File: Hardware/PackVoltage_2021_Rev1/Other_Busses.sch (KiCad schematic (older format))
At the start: 50 parts, among them Q10 Q_NMOS_DGS, Q6 Q_NMOS_DGS, Q7 Q_NMOS_DGS, Q8 Q_NMOS_DGS, Q9 Q_NMOS_DGS, U14 LT1910, U15 LT1910, U16 LT1910, U17 INA281, U18 INA281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

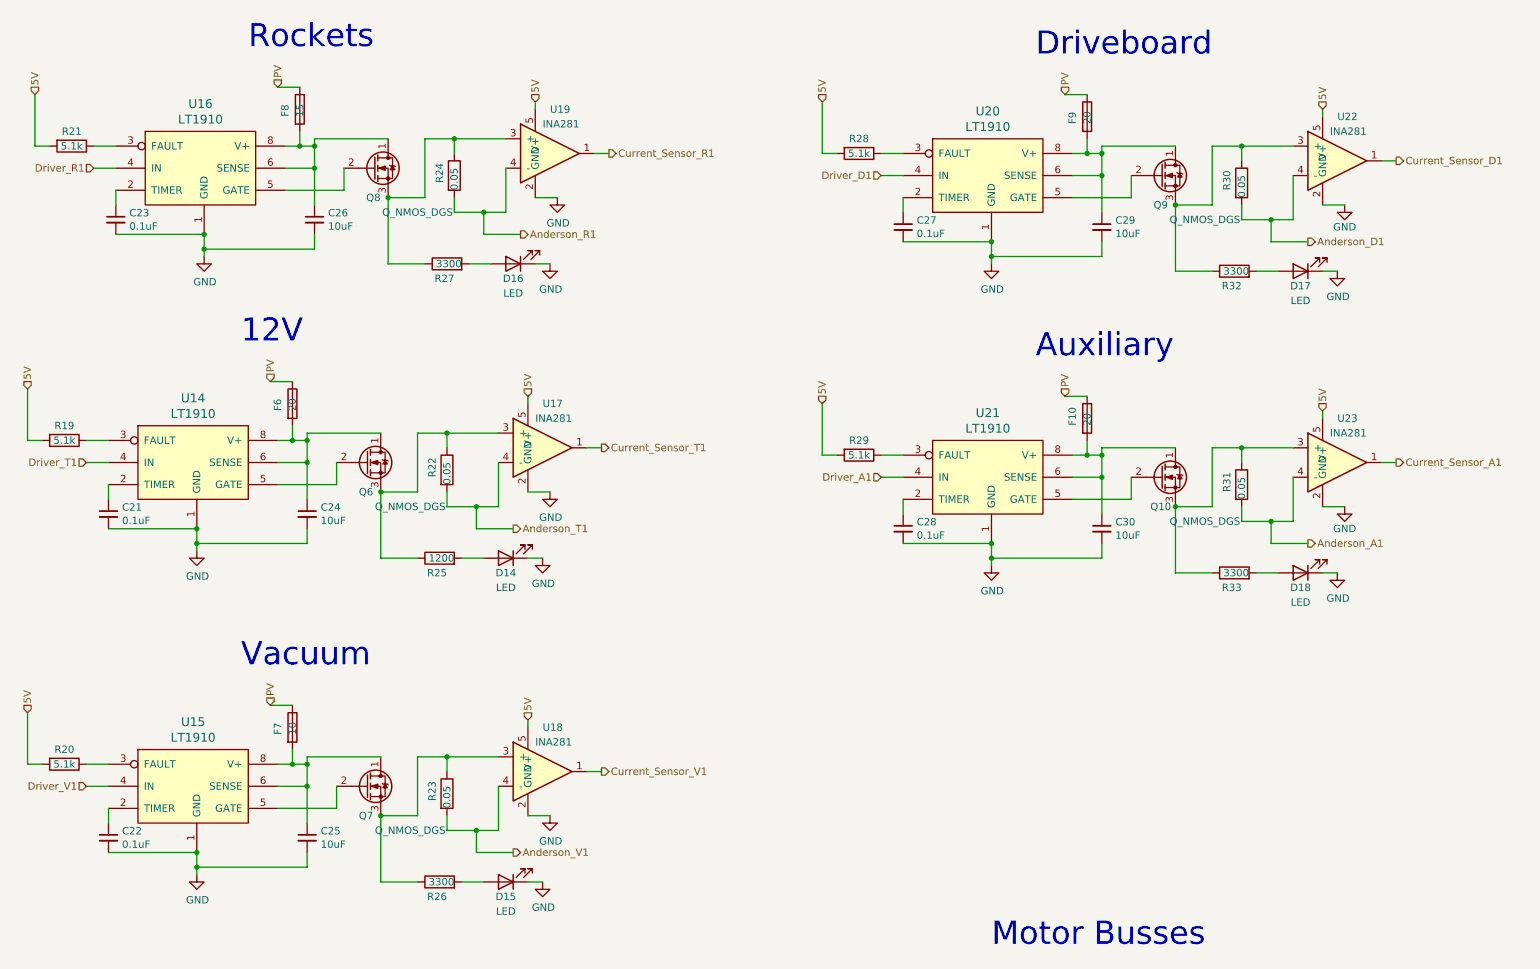
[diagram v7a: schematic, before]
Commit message: Updated 12 Molex, Changed Shunt Resistors
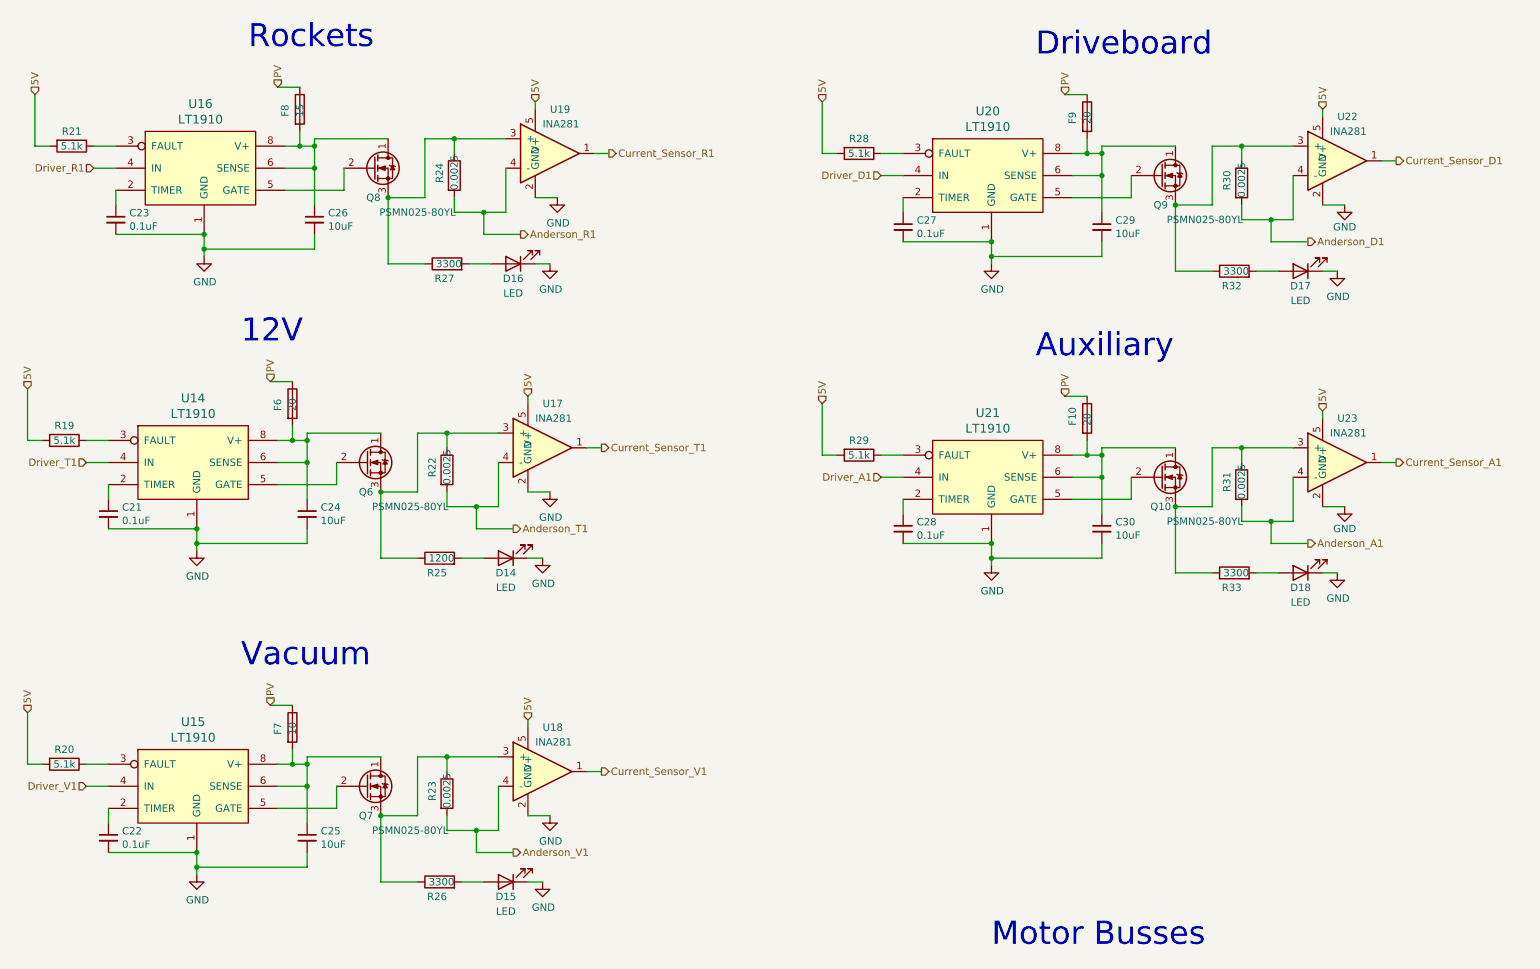
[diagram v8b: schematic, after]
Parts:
- Q10, Q6, Q7, Q8, Q9: value Q_NMOS_DGS -> PSMN025-80YL
- R22, R23, R24, R30, R31: value 0.05 -> 0.0025; footprint Resistor_SMD:R_2512_6332Metric_Pad1.40x3.35mm_HandSolder -> Resistor_SMD:R_2512_6332Metric_Pad1.52x3.35mm_HandSolder
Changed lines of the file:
@@
 AR Path="/5F8EFCC9/5F768EE8" Ref="Q8"  Part="1"
 F 0 "Q8" H 3000 1450 50  0000 C CNN
-F 1 "Q_NMOS_DGS" H 3300 1350 50  0000 C CNN
+F 1 "PSMN025-80YL" H 3300 1350 50  0000 C CNN
 F 2 "Custom:LFPAK56_MOSFET" H 3200 1750 50  0001 C CNN
 F 3 "~" H 3000 1650 50  0001 C CNN
@@
 AR Path="/5F8EFCC9/5F9AF790" Ref="R24"  Part="1"
 F 0 "R24" V 3450 1650 50  0000 L CNN
-F 1 "0.05" V 3550 1600 50  0000 L CNN
-F 2 "Resistor_SMD:R_2512_6332Metric_Pad1.40x3.35mm_HandSolder" V 3480 1700 50  0001 C CNN
+F 1 "0.0025" V 3550 1600 50  0000 L CNN
+F 2 "Resistor_SMD:R_2512_6332Metric_Pad1.52x3.35mm_HandSolder" V 3480 1700 50  0001 C CNN
 F 3 "https://riedon.com/media/pdf/PFS35.pdf" H 3550 1700 50  0001 C CNN
 	1    3550 1700
@@
 AR Path="/5F8EFCC9/5F9AF794" Ref="Q6"  Part="1"
 F 0 "Q6" H 2950 3450 50  0000 C CNN
-F 1 "Q_NMOS_DGS" H 3250 3350 50  0000 C CNN
+F 1 "PSMN025-80YL" H 3250 3350 50  0000 C CNN
 F 2 "Custom:LFPAK56_MOSFET" H 3150 3750 50  0001 C CNN
 F 3 "~" H 2950 3650 50  0001 C CNN
@@
 AR Path="/5F8EFCC9/5F9AF79A" Ref="R22"  Part="1"
 F 0 "R22" V 3400 3650 50  0000 L CNN
-F 1 "0.05" V 3500 3600 50  0000 L CNN
-F 2 "Resistor_SMD:R_2512_6332Metric_Pad1.40x3.35mm_HandSolder" V 3430 3700 50  0001 C CNN
+F 1 "0.0025" V 3500 3600 50  0000 L CNN
+F 2 "Resistor_SMD:R_2512_6332Metric_Pad1.52x3.35mm_HandSolder" V 3430 3700 50  0001 C CNN
 F 3 "https://riedon.com/media/pdf/PFS35.pdf" H 3500 3700 50  0001 C CNN
 	1    3500 3700
@@
 AR Path="/5F8EFCC9/5F9AF7A1" Ref="Q7"  Part="1"
 F 0 "Q7" H 2950 5650 50  0000 C CNN
-F 1 "Q_NMOS_DGS" H 3250 5550 50  0000 C CNN
+F 1 "PSMN025-80YL" H 3250 5550 50  0000 C CNN
 F 2 "Custom:LFPAK56_MOSFET" H 3150 5950 50  0001 C CNN
 F 3 "~" H 2950 5850 50  0001 C CNN
@@
 AR Path="/5F8EFCC9/5F8A5A13" Ref="R23"  Part="1"
 F 0 "R23" V 3400 5850 50  0000 L CNN
-F 1 "0.05" V 3500 5800 50  0000 L CNN
-F 2 "Resistor_SMD:R_2512_6332Metric_Pad1.40x3.35mm_HandSolder" V 3430 5900 50  0001 C CNN
+F 1 "0.0025" V 3500 5800 50  0000 L CNN
+F 2 "Resistor_SMD:R_2512_6332Metric_Pad1.52x3.35mm_HandSolder" V 3430 5900 50  0001 C CNN
 F 3 "https://riedon.com/media/pdf/PFS35.pdf" H 3500 5900 50  0001 C CNN
 	1    3500 5900
@@
 AR Path="/5F8EFCC9/5F8B2B16" Ref="Q9"  Part="1"
 F 0 "Q9" H 8350 1500 50  0000 C CNN
-F 1 "Q_NMOS_DGS" H 8650 1400 50  0000 C CNN
+F 1 "PSMN025-80YL" H 8650 1400 50  0000 C CNN
 F 2 "Custom:LFPAK56_MOSFET" H 8550 1800 50  0001 C CNN
 F 3 "~" H 8350 1700 50  0001 C CNN
@@
 AR Path="/5F8EFCC9/5F8B2B66" Ref="R30"  Part="1"
 F 0 "R30" V 8800 1700 50  0000 L CNN
-F 1 "0.05" V 8900 1650 50  0000 L CNN
-F 2 "Resistor_SMD:R_2512_6332Metric_Pad1.40x3.35mm_HandSolder" V 8830 1750 50  0001 C CNN
+F 1 "0.0025" V 8900 1650 50  0000 L CNN
+F 2 "Resistor_SMD:R_2512_6332Metric_Pad1.52x3.35mm_HandSolder" V 8830 1750 50  0001 C CNN
 F 3 "https://riedon.com/media/pdf/PFS35.pdf" H 8900 1750 50  0001 C CNN
 	1    8900 1750
@@
 AR Path="/5F8EFCC9/5F8E41E6" Ref="Q10"  Part="1"
 F 0 "Q10" H 8350 3550 50  0000 C CNN
-F 1 "Q_NMOS_DGS" H 8650 3450 50  0000 C CNN
+F 1 "PSMN025-80YL" H 8650 3450 50  0000 C CNN
 F 2 "Custom:LFPAK56_MOSFET" H 8550 3850 50  0001 C CNN
 F 3 "~" H 8350 3750 50  0001 C CNN
@@
 AR Path="/5F8EFCC9/5F8E4229" Ref="R31"  Part="1"
 F 0 "R31" V 8800 3750 50  0000 L CNN
-F 1 "0.05" V 8900 3700 50  0000 L CNN
-F 2 "Resistor_SMD:R_2512_6332Metric_Pad1.40x3.35mm_HandSolder" V 8830 3800 50  0001 C CNN
+F 1 "0.0025" V 8900 3700 50  0000 L CNN
+F 2 "Resistor_SMD:R_2512_6332Metric_Pad1.52x3.35mm_HandSolder" V 8830 3800 50  0001 C CNN
 F 3 "https://riedon.com/media/pdf/PFS35.pdf" H 8900 3800 50  0001 C CNN
 	1    8900 3800
